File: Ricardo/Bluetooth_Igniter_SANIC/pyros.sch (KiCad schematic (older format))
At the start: 20 parts

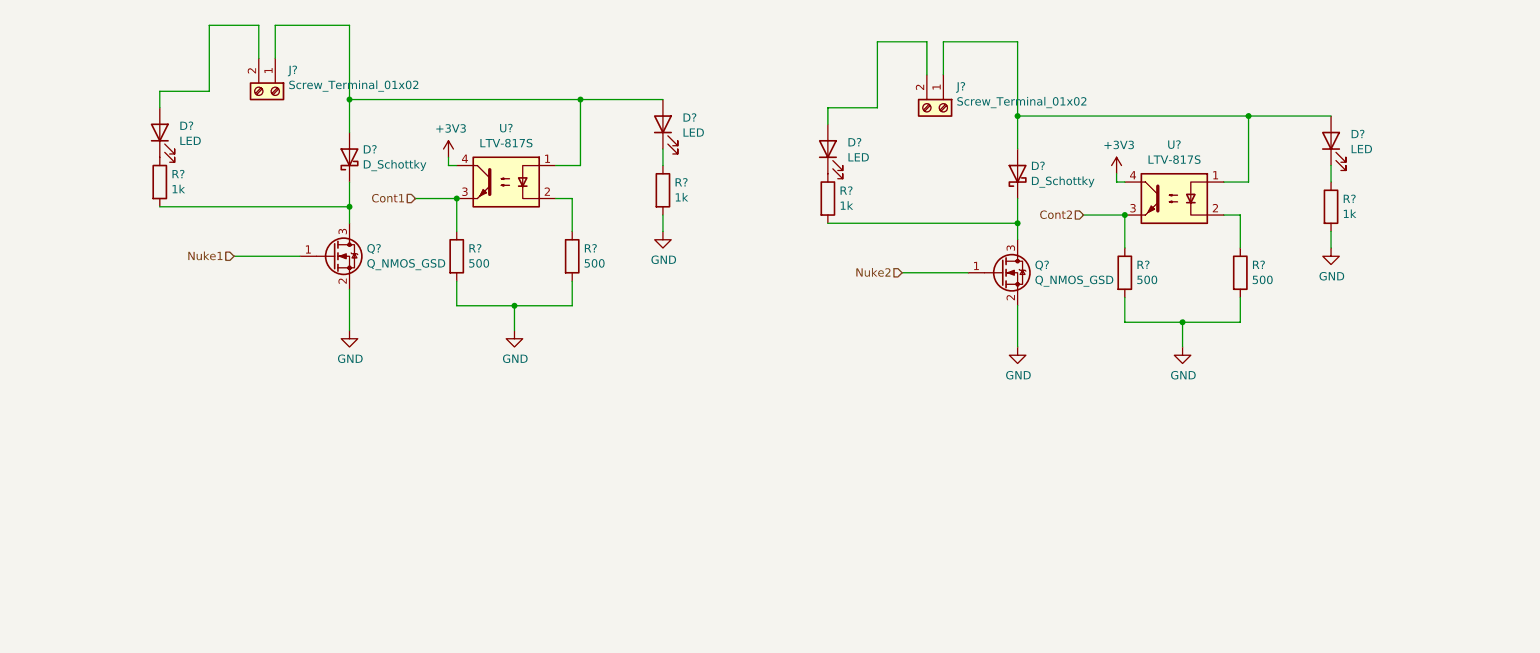
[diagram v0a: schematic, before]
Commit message: updated
sized voltage regulator components
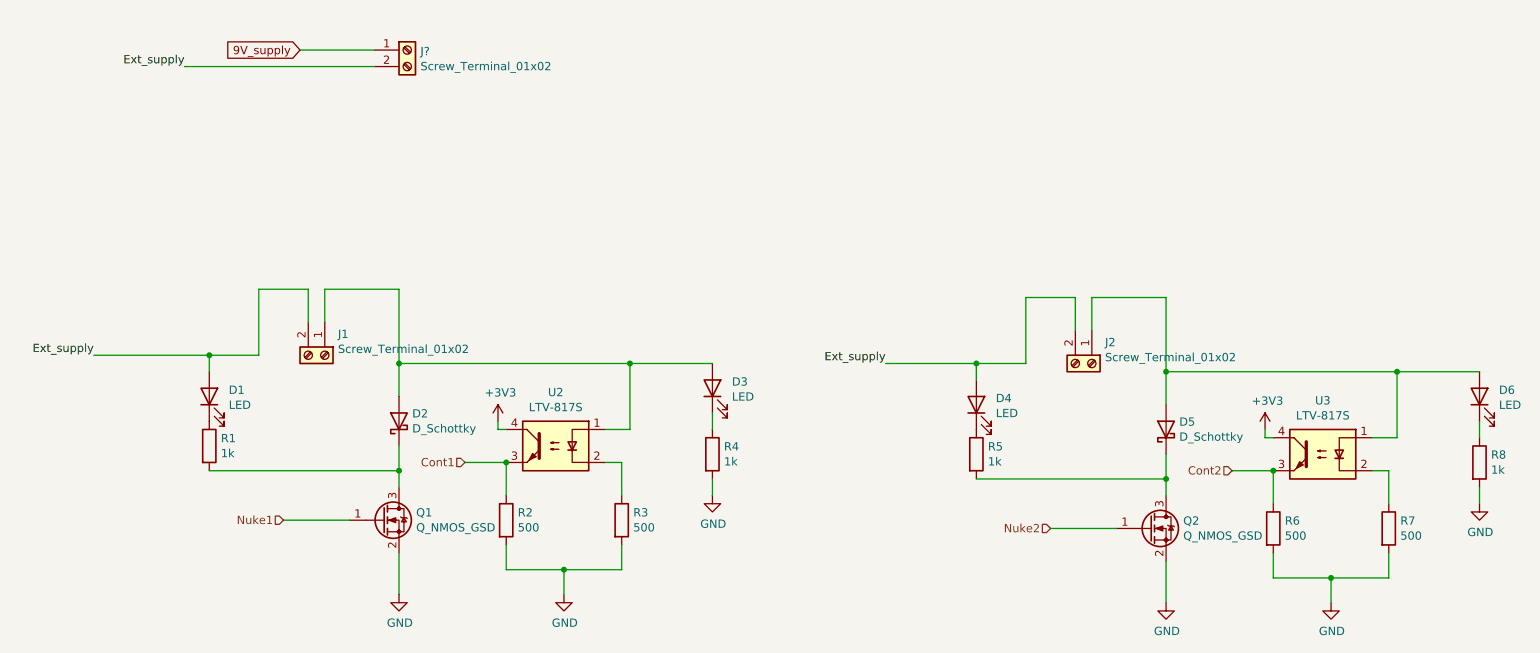
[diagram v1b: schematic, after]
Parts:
- added J?: Screw_Terminal_01x02, symbol Connector:Screw_Terminal_01x02
- D2: renamed from D?; footprint (none) -> Diode_SMD:D_SOD-123F
- D3: renamed from D?; footprint (none) -> LED_SMD:LED_0603_1608Metric_Castellated
- Q1: renamed from Q?; footprint (none) -> Package_TO_SOT_SMD:SOT-23
- R4, R5: renamed from R?; footprint (none) -> Resistor_SMD:R_0603_1608Metric
- gave numbers to parts that had none: 15
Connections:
- net Ext_supply: now reaches D1.2 (A), J1.2 (Pin_2)
- net Ext_supply: now also D4.2 (A), J2.2 (Pin_2), J?.2 (Pin_2)
- new net 9V_supply: J?.1 (Pin_1)
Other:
- moved on the sheet: D1, D2, D3, D4, D5, D6, J1, J2, Q1, Q2, R1, R2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

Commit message: Added USB
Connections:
- net 9V_supply renamed VDD
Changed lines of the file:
@@
 $Descr A4 11693 8268
 encoding utf-8
-Sheet 2 3
+Sheet 2 4
 Title ""
 Date ""
@@
 Wire Wire Line
 	3200 1700 2750 1700
-Text GLabel 2750 1700 0    50   Input ~ 0
-9V_supply
+$Comp
+L power:VDD #PWR?
+U 1 1 604B3741
+P 2750 1700
+F 0 "#PWR?" H 2750 1550 50  0001 C CNN
+F 1 "VDD" H 2765 1873 50  0000 C CNN
+F 2 "" H 2750 1700 50  0001 C CNN
+F 3 "" H 2750 1700 50  0001 C CNN
+	1    2750 1700
+	1    0    0    -1
+$EndComp
 $EndSCHEMATC

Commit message: Finished schematic; starting pcb design
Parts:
- D4: renamed from D1; footprint (none) -> LED_SMD:LED_0603_1608Metric_Castellated
- D7: renamed from D4; footprint (none) -> LED_SMD:LED_0603_1608Metric_Castellated
- D8: renamed from D5; footprint (none) -> Diode_SMD:D_SOD-123F
- D9: renamed from D6; footprint (none) -> LED_SMD:LED_0603_1608Metric_Castellated
- J1: footprint (none) -> iclrhw:PHOENIX_1757242
- J2: renamed from J?; footprint (none) -> iclrhw:PHOENIX_1757242
- J3: renamed from J2; footprint (none) -> iclrhw:PHOENIX_1757242
- Q4: renamed from Q2; footprint (none) -> Package_TO_SOT_SMD:SOT-23
- R11: renamed from R1; footprint (none) -> Resistor_SMD:R_0603_1608Metric
- R12: renamed from R2; footprint (none) -> Resistor_SMD:R_0603_1608Metric
- R13: renamed from R3; footprint (none) -> Resistor_SMD:R_0603_1608Metric
- R16: renamed from R6; footprint (none) -> Resistor_SMD:R_0603_1608Metric
- R17: renamed from R7; footprint (none) -> Resistor_SMD:R_0603_1608Metric
- R18: renamed from R8; footprint (none) -> Resistor_SMD:R_0603_1608Metric
- renumbered D2 to D5, D3 to D6, Q1 to Q3, R4 to R14, R5 to R15, U2 to U3, U3 to U4
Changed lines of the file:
@@
 $Descr A4 11693 8268
 encoding utf-8
-Sheet 2 4
+Sheet 4 4
 Title ""
 Date ""
@@
 F 0 "J1" V 2772 3630 50  0000 L CNN
 F 1 "Screw_Terminal_01x02" V 2863 3630 50  0000 L CNN
-F 2 "" H 2900 3550 50  0001 C CNN
+F 2 "iclrhw:PHOENIX_1757242" H 2900 3550 50  0001 C CNN
 F 3 "~" H 2900 3550 50  0001 C CNN
 	1    2900 3550
@@
 	2200 3550 2200 3650
 $Comp
-L Device:LED D1
+L Device:LED D4
 U 1 1 603A73D6
 P 2200 3800
-F 0 "D1" V 2239 3682 50  0000 R CNN
+F 0 "D4" V 2239 3682 50  0000 R CNN
 F 1 "LED" V 2148 3682 50  0000 R CNN
-F 2 "" H 2200 3800 50  0001 C CNN
+F 2 "LED_SMD:LED_0603_1608Metric_Castellated" H 2200 3800 50  0001 C CNN
 F 3 "~" H 2200 3800 50  0001 C CNN
 	1    2200 3800
@@
 $EndComp
 $Comp
-L Device:R R1
+L Device:R R11
 U 1 1 603A9084
 P 2200 4100
-F 0 "R1" H 2270 4146 50  0000 L CNN
+F 0 "R11" H 2270 4146 50  0000 L CNN
 F 1 "1k" H 2270 4055 50  0000 L CNN
-F 2 "" V 2130 4100 50  0001 C CNN
+F 2 "Resistor_SMD:R_0603_1608Metric" V 2130 4100 50  0001 C CNN
 F 3 "~" H 2200 4100 50  0001 C CNN
 	1    2200 4100
@@
 	2900 3150 3350 3150
 $Comp
-L Device:D_Schottky D2
+L Device:D_Schottky D5
 U 1 1 603AA2C9
 P 3350 3950
-F 0 "D2" V 3396 3870 50  0000 R CNN
+F 0 "D5" V 3396 3870 50  0000 R CNN
 F 1 "D_Schottky" V 3305 3870 50  0000 R CNN
 F 2 "Diode_SMD:D_SOD-123F" H 3350 3950 50  0001 C CNN
@@
 	3350 4100 3350 4250
 $Comp
-L Device:Q_NMOS_GSD Q1
+L Device:Q_NMOS_GSD Q3
 U 1 1 603AC2C0
 P 3250 4550
-F 0 "Q1" H 3454 4596 50  0000 L CNN
+F 0 "Q3" H 3454 4596 50  0000 L CNN
 F 1 "Q_NMOS_GSD" H 3454 4505 50  0000 L CNN
 F 2 "Package_TO_SOT_SMD:SOT-23" H 3450 4650 50  0001 C CNN
@@
 	3350 4750 3350 5000
 $Comp
-L power:GND #PWR0103
+L power:GND #PWR016
 U 1 1 603AD57D
 P 3350 5000
-F 0 "#PWR0103" H 3350 4750 50  0001 C CNN
+F 0 "#PWR016" H 3350 4750 50  0001 C CNN
 F 1 "GND" H 3355 4827 50  0000 C CNN
 F 2 "" H 3350 5000 50  0001 C CNN
@@
 Wire Wire Line
 	2650 4550 3050 4550
-Text HLabel 2650 4550 0    50   Input ~ 0
-Nuke1
 Wire Wire Line
 	4750 3600 5250 3600
@@
 	4700 4200 4700 4400
 $Comp
-L Device:R R3
+L Device:R R13
 U 1 1 603BD235
 P 4700 4550
-F 0 "R3" H 4770 4596 50  0000 L CNN
+F 0 "R13" H 4770 4596 50  0000 L CNN
 F 1 "500" H 4770 4505 50  0000 L CNN
-F 2 "" V 4630 4550 50  0001 C CNN
+F 2 "Resistor_SMD:R_0603_1608Metric" V 4630 4550 50  0001 C CNN
 F 3 "~" H 4700 4550 50  0001 C CNN
 	1    4700 4550
@@
 	4750 4000 4600 4000
 $Comp
-L Isolator:LTV-817S U2
+L Isolator:LTV-817S U3
 U 1 1 603B55A8
 P 4300 4100
-F 0 "U2" H 4300 4425 50  0000 C CNN
+F 0 "U3" H 4300 4425 50  0000 C CNN
 F 1 "LTV-817S" H 4300 4334 50  0000 C CNN
 F 2 "Package_DIP:SMDIP-4_W9.53mm" H 4300 3800 50  0001 C CNN
@@
 	4000 4200 3750 4200
 $Comp
-L Device:R R2
+L Device:R R12
 U 1 1 603C08B5
 P 4000 4550
-F 0 "R2" H 4070 4596 50  0000 L CNN
+F 0 "R12" H 4070 4596 50  0000 L CNN
 F 1 "500" H 4070 4505 50  0000 L CNN
-F 2 "" V 3930 4550 50  0001 C CNN
+F 2 "Resistor_SMD:R_0603_1608Metric" V 3930 4550 50  0001 C CNN
 F 3 "~" H 4000 4550 50  0001 C CNN
 	1    4000 4550
@@
 	4350 4850 4350 5000
 $Comp
-L power:GND #PWR0104
+L power:GND #PWR018
 U 1 1 603C2975
 P 4350 5000
-F 0 "#PWR0104" H 4350 4750 50  0001 C CNN
+F 0 "#PWR018" H 4350 4750 50  0001 C CNN
 F 1 "GND" H 4355 4827 50  0000 C CNN
 F 2 "" H 4350 5000 50  0001 C CNN
@@
 $EndComp
 $Comp
-L Device:LED D3
+L Device:LED D6
 U 1 1 603C55BC
 P 5250 3750
-F 0 "D3" V 5289 3632 50  0000 R CNN
+F 0 "D6" V 5289 3632 50  0000 R CNN
 F 1 "LED" V 5198 3632 50  0000 R CNN
 F 2 "LED_SMD:LED_0603_1608Metric_Castellated" H 5250 3750 50  0001 C CNN
@@
 	5250 3900 5250 4000
 $Comp
-L Device:R R4
+L Device:R R14
 U 1 1 603C7858
 P 5250 4150
-F 0 "R4" H 5320 4196 50  0000 L CNN
+F 0 "R14" H 5320 4196 50  0000 L CNN
 F 1 "1k" H 5320 4105 50  0000 L CNN
 F 2 "Resistor_SMD:R_0603_1608Metric" V 5180 4150 50  0001 C CNN
@@
 $EndComp
 $Comp
-L power:GND #PWR0105
+L power:GND #PWR019
 U 1 1 603C83CD
 P 5250 4400
-F 0 "#PWR0105" H 5250 4150 50  0001 C CNN
+F 0 "#PWR019" H 5250 4150 50  0001 C CNN
 F 1 "GND" H 5255 4227 50  0000 C CNN
 F 2 "" H 5250 4400 50  0001 C CNN
@@
 	5250 4300 5250 4400
 $Comp
-L power:+3V3 #PWR0106
+L power:+3V3 #PWR017
 U 1 1 603C95D6
 P 3950 3950
-F 0 "#PWR0106" H 3950 3800 50  0001 C CNN
+F 0 "#PWR017" H 3950 3800 50  0001 C CNN
 F 1 "+3V3" H 3965 4123 50  0000 C CNN
 F 2 "" H 3950 3950 50  0001 C CNN
@@
 	3350 3600 3350 3800
 $Comp
-L Connector:Screw_Terminal_01x02 J2
+L Connector:Screw_Terminal_01x02 J3
 U 1 1 603DB3E4
 P 7550 3600
-F 0 "J2" V 7422 3680 50  0000 L CNN
+F 0 "J3" V 7422 3680 50  0000 L CNN
 F 1 "Screw_Terminal_01x02" V 7513 3680 50  0000 L CNN
-F 2 "" H 7550 3600 50  0001 C CNN
+F 2 "iclrhw:PHOENIX_1757242" H 7550 3600 50  0001 C CNN
 F 3 "~" H 7550 3600 50  0001 C CNN
 	1    7550 3600
@@
 	6850 3600 6850 3700
 $Comp
-L Device:LED D4
+L Device:LED D7
 U 1 1 603DB539
 P 6850 3850
-F 0 "D4" V 6889 3732 50  0000 R CNN
+F 0 "D7" V 6889 3732 50  0000 R CNN
 F 1 "LED" V 6798 3732 50  0000 R CNN
-F 2 "" H 6850 3850 50  0001 C CNN
+F 2 "LED_SMD:LED_0603_1608Metric_Castellated" H 6850 3850 50  0001 C CNN
 F 3 "~" H 6850 3850 50  0001 C CNN
 	1    6850 3850
@@
 $EndComp
 $Comp
-L Device:R R5
+L Device:R R15
 U 1 1 603DB543
 P 6850 4150
-F 0 "R5" H 6920 4196 50  0000 L CNN
+F 0 "R15" H 6920 4196 50  0000 L CNN
 F 1 "1k" H 6920 4105 50  0000 L CNN
 F 2 "Resistor_SMD:R_0603_1608Metric" V 6780 4150 50  0001 C CNN
@@
 	7550 3200 8000 3200
 $Comp
-L Device:D_Schottky D5
+L Device:D_Schottky D8
 U 1 1 603DB54F
 P 8000 4000
-F 0 "D5" V 8046 3920 50  0000 R CNN
+F 0 "D8" V 8046 3920 50  0000 R CNN
 F 1 "D_Schottky" V 7955 3920 50  0000 R CNN
-F 2 "" H 8000 4000 50  0001 C CNN
+F 2 "Diode_SMD:D_SOD-123F" H 8000 4000 50  0001 C CNN
 F 3 "~" H 8000 4000 50  0001 C CNN
 	1    8000 4000
@@
 	8000 4150 8000 4300
 $Comp
-L Device:Q_NMOS_GSD Q2
+L Device:Q_NMOS_GSD Q4
 U 1 1 603DB55B
 P 7900 4600
-F 0 "Q2" H 8104 4646 50  0000 L CNN
+F 0 "Q4" H 8104 4646 50  0000 L CNN
 F 1 "Q_NMOS_GSD" H 8104 4555 50  0000 L CNN
-F 2 "" H 8100 4700 50  0001 C CNN
+F 2 "Package_TO_SOT_SMD:SOT-23" H 8100 4700 50  0001 C CNN
 F 3 "~" H 7900 4600 50  0001 C CNN
 	1    7900 4600
@@
 	8000 4800 8000 5050
 $Comp
-L power:GND #PWR0107
+L power:GND #PWR020
 U 1 1 603DB566
 P 8000 5050
-F 0 "#PWR0107" H 8000 4800 50  0001 C CNN
+F 0 "#PWR020" H 8000 4800 50  0001 C CNN
 F 1 "GND" H 8005 4877 50  0000 C CNN
 F 2 "" H 8000 5050 50  0001 C CNN
@@
 	9350 4250 9350 4450
 $Comp
-L Device:R R7
+L Device:R R17
 U 1 1 603DB575
 P 9350 4600
-F 0 "R7" H 9420 4646 50  0000 L CNN
+F 0 "R17" H 9420 4646 50  0000 L CNN
 F 1 "500" H 9420 4555 50  0000 L CNN
-F 2 "" V 9280 4600 50  0001 C CNN
+F 2 "Resistor_SMD:R_0603_1608Metric" V 9280 4600 50  0001 C CNN
 F 3 "~" H 9350 4600 50  0001 C CNN
 	1    9350 4600
@@
 	9400 4050 9250 4050
 $Comp
-L Isolator:LTV-817S U3
+L Isolator:LTV-817S U4
 U 1 1 603DB582
 P 8950 4150
-F 0 "U3" H 8950 4475 50  0000 C CNN
+F 0 "U4" H 8950 4475 50  0000 C CNN
 F 1 "LTV-817S" H 8950 4384 50  0000 C CNN
 F 2 "Package_DIP:SMDIP-4_W9.53mm" H 8950 3850 50  0001 C CNN
@@
 	8650 4250 8400 4250
 $Comp
-L Device:R R6
+L Device:R R16
 U 1 1 603DB590
 P 8650 4600
-F 0 "R6" H 8720 4646 50  0000 L CNN
+F 0 "R16" H 8720 4646 50  0000 L CNN
 F 1 "500" H 8720 4555 50  0000 L CNN
-F 2 "" V 8580 4600 50  0001 C CNN
+F 2 "Resistor_SMD:R_0603_1608Metric" V 8580 4600 50  0001 C CNN
 F 3 "~" H 8650 4600 50  0001 C CNN
 	1    8650 4600
@@
 	9000 4900 9000 5050
 $Comp
-L power:GND #PWR0108
+L power:GND #PWR022
 U 1 1 603DB59F
 P 9000 5050
-F 0 "#PWR0108" H 9000 4800 50  0001 C CNN
+F 0 "#PWR022" H 9000 4800 50  0001 C CNN
 F 1 "GND" H 9005 4877 50  0000 C CNN
 F 2 "" H 9000 5050 50  0001 C CNN
@@
 $EndComp
 $Comp
-L Device:LED D6
+L Device:LED D9
 U 1 1 603DB5A9
 P 9900 3800
-F 0 "D6" V 9939 3682 50  0000 R CNN
+F 0 "D9" V 9939 3682 50  0000 R CNN
 F 1 "LED" V 9848 3682 50  0000 R CNN
-F 2 "" H 9900 3800 50  0001 C CNN
+F 2 "LED_SMD:LED_0603_1608Metric_Castellated" H 9900 3800 50  0001 C CNN
 F 3 "~" H 9900 3800 50  0001 C CNN
 	1    9900 3800
@@
 	9900 3950 9900 4050
 $Comp
-L Device:R R8
+L Device:R R18
 U 1 1 603DB5B4
 P 9900 4200
-F 0 "R8" H 9970 4246 50  0000 L CNN
+F 0 "R18" H 9970 4246 50  0000 L CNN
 F 1 "1k" H 9970 4155 50  0000 L CNN
-F 2 "" V 9830 4200 50  0001 C CNN
+F 2 "Resistor_SMD:R_0603_1608Metric" V 9830 4200 50  0001 C CNN
 F 3 "~" H 9900 4200 50  0001 C CNN
 	1    9900 4200
@@
 $EndComp
 $Comp
-L power:GND #PWR0109
+L power:GND #PWR023
 U 1 1 603DB5BE
 P 9900 4450
-F 0 "#PWR0109" H 9900 4200 50  0001 C CNN
+F 0 "#PWR023" H 9900 4200 50  0001 C CNN
 F 1 "GND" H 9905 4277 50  0000 C CNN
 F 2 "" H 9900 4450 50  0001 C CNN
@@
 	9900 4350 9900 4450
 $Comp
-L power:+3V3 #PWR0110
+L power:+3V3 #PWR021
 U 1 1 603DB5C9
 P 8600 4000
-F 0 "#PWR0110" H 8600 3850 50  0001 C CNN
+F 0 "#PWR021" H 8600 3850 50  0001 C CNN
 F 1 "+3V3" H 8615 4173 50  0000 C CNN
 F 2 "" H 8600 4000 50  0001 C CNN
@@
 Connection ~ 6850 3600
 $Comp
-L Connector:Screw_Terminal_01x02 J?
+L Connector:Screw_Terminal_01x02 J2
 U 1 1 6047AC74
 P 3400 1700
-F 0 "J?" H 3480 1692 50  0000 L CNN
+F 0 "J2" H 3480 1692 50  0000 L CNN
 F 1 "Screw_Terminal_01x02" H 3480 1601 50  0000 L CNN
-F 2 "" H 3400 1700 50  0001 C CNN
+F 2 "iclrhw:PHOENIX_1757242" H 3400 1700 50  0001 C CNN
 F 3 "~" H 3400 1700 50  0001 C CNN
 	1    3400 1700
@@
 	3200 1700 2750 1700
 $Comp
-L power:VDD #PWR?
+L power:VDD #PWR015
 U 1 1 604B3741
 P 2750 1700
-F 0 "#PWR?" H 2750 1550 50  0001 C CNN
+F 0 "#PWR015" H 2750 1550 50  0001 C CNN
 F 1 "VDD" H 2765 1873 50  0000 C CNN
 F 2 "" H 2750 1700 50  0001 C CNN
@@
 	1    0    0    -1
 $EndComp
+Text HLabel 2650 4550 0    50   Input ~ 0
+Nuke1
 $EndSCHEMATC
